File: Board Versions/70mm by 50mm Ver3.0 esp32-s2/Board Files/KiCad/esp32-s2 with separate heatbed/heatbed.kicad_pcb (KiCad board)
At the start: 2 copper layers, 87.9 x 60.2 mm, 5 parts

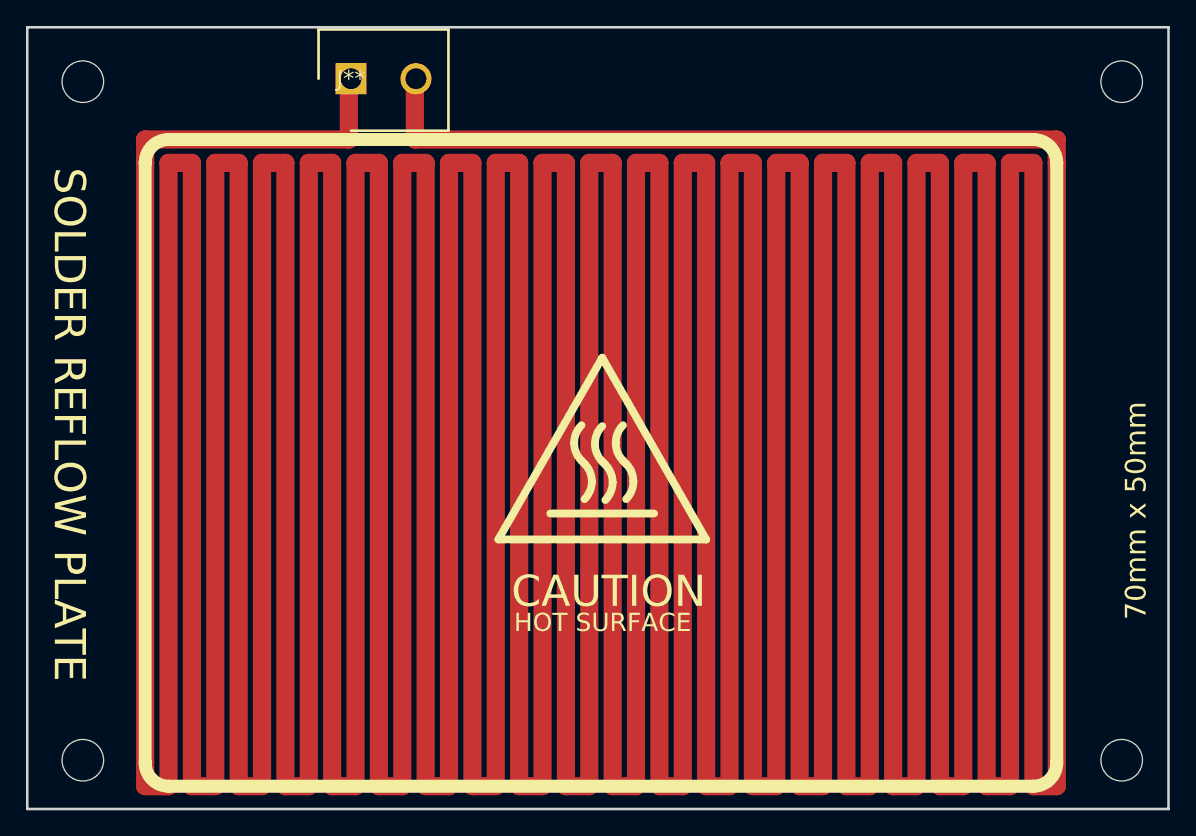
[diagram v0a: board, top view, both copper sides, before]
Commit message: Higher resistance heatbed
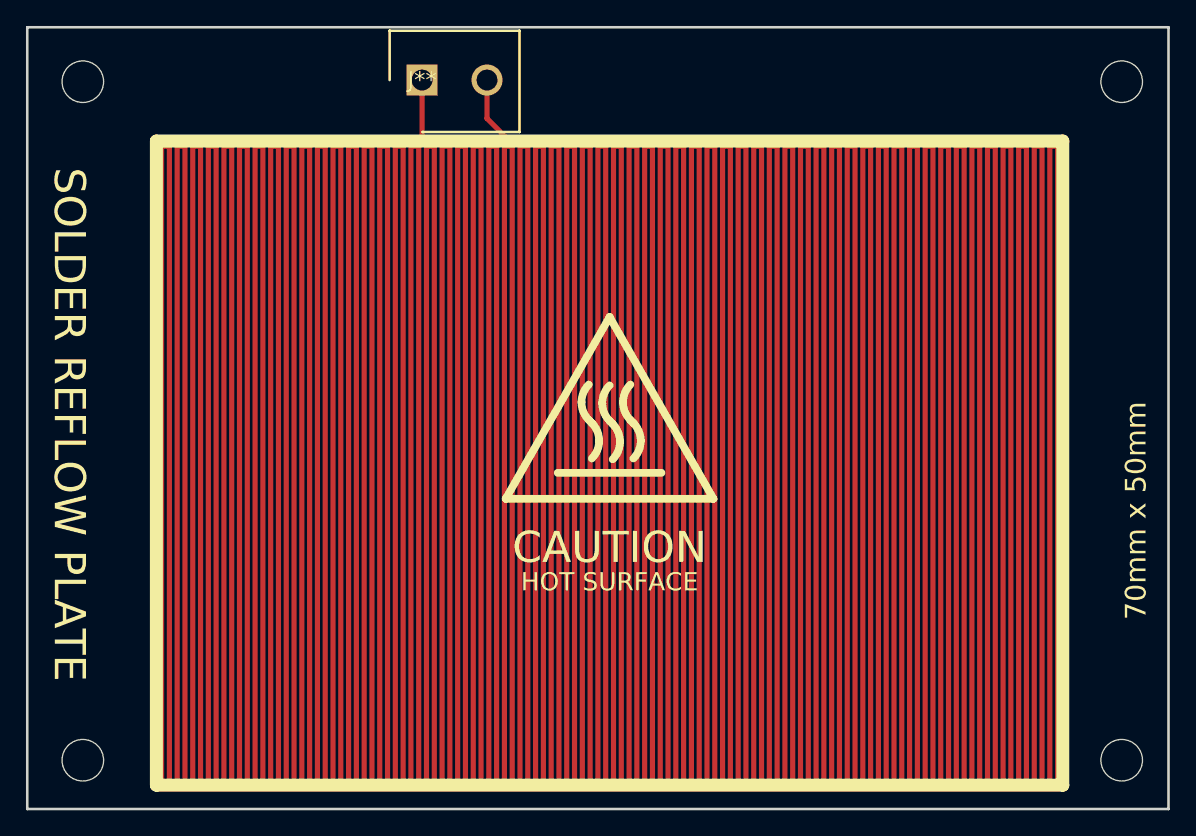
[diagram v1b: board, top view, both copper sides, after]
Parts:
- moved J** 5.47 mm to (38.0, 90.4)
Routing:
- net (no net): track 0.00 -> 5973.9 mm
- net VCC: track 2068.0 -> 0.00 mm
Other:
- board text removed: "github.com/AfterEarthLTD/Solder-Reflow-Plate"
